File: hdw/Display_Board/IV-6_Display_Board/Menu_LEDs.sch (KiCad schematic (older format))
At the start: 1 part

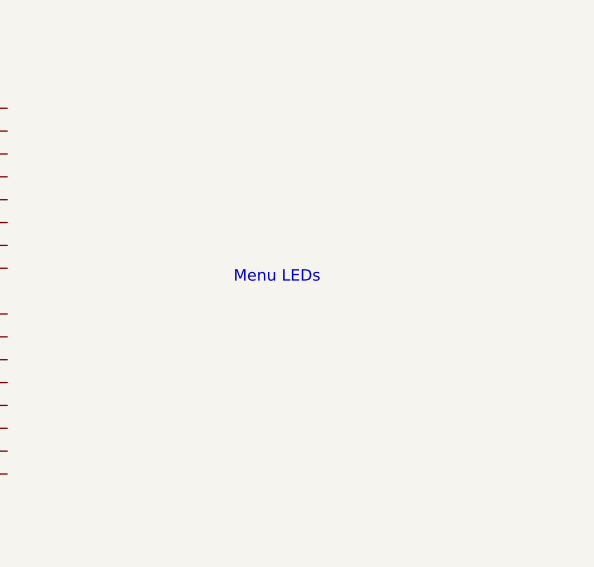
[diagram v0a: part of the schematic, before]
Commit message: Added backup RTC, IO connector, other stuff
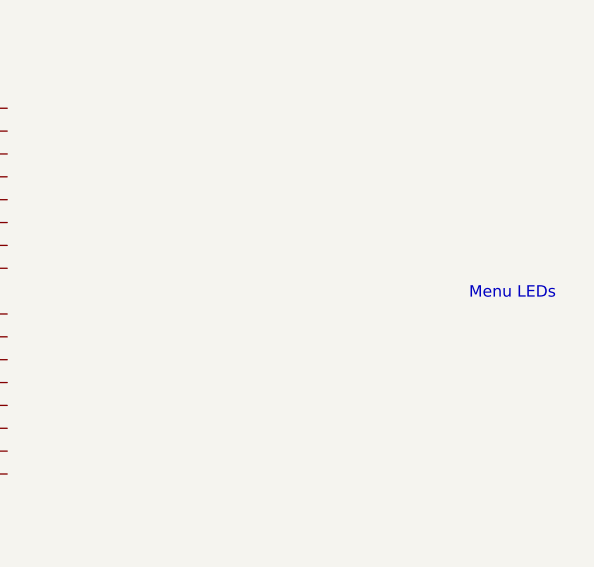
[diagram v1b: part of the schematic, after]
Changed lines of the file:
@@
 EESchema Schematic File Version 4
+LIBS:IV-6_Display_Board-cache
 EELAYER 30 0
 EELAYER END
 $Descr A 11000 8500
 encoding utf-8
-Sheet 5 5
+Sheet 5 7
 Title ""
 Date ""
@@
 Text GLabel 4360 2610 0    50   Input ~ 0
 I2C_DSP_SCL
-Text Notes 6750 3280 0    50   ~ 0
+Text Notes 7780 3350 0    50   ~ 0
 Menu LEDs
 $EndSCHEMATC

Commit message: Display board tweaks, added buzzer, other stuff
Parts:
- added C?: 0.1uF, Capacitors_SMD:C_0603, symbol Custom_Library:C_Custom
- added DOC?: I2C_Address, symbol Custom_Library:I2C_Address
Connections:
- net +5V: now also C?.1
- net GND: now also C?.2
- net Display_Time_LED: now reaches U?.1 (P00)
- net 24HR_Mode_LED: now reaches U?.10 (P10)
- net Alarm_Enable_LED: now reaches U?.11 (P11)
- net Set_Time_LED: now reaches U?.2 (P01)
- net Display_Date_LED: now reaches U?.3 (P02)
- net Set_Date_LED: now reaches U?.4 (P03)
- net Display_Weekday_LED: now reaches U?.5 (P04)
- net Set_Weekday_LED: now reaches U?.6 (P05)
- net Display_Alarm_LED: now reaches U?.7 (P06)
- net Set_Alarm_LED: now reaches U?.8 (P07)
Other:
- note removed: "Menu LEDs"
- moved on the sheet: U?
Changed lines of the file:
@@
 $Descr A 11000 8500
 encoding utf-8
-Sheet 5 9
+Sheet 5 12
 Title ""
 Date ""
@@
 L Interface_Expansion:TCA9555RGER U?
 U 1 1 5E0AA272
-P 5060 3310
-F 0 "U?" H 4610 4260 50  0000 C CNN
-F 1 "TCA9555RGER" H 5060 3310 50  0000 C CNN
-F 2 "Package_DFN_QFN:QFN-24-1EP_4x4mm_P0.5mm_EP2.6x2.6mm" H 6260 2310 50  0001 C CNN
-F 3 "http://www.ti.com/lit/ds/symlink/tca9555.pdf" H 4560 4210 50  0001 C CNN
-	1    5060 3310
+P 2960 3100
+F 0 "U?" H 2510 4050 50  0000 C CNN
+F 1 "TCA9555RGER" H 2960 3100 50  0000 C CNN
+F 2 "Package_DFN_QFN:QFN-24-1EP_4x4mm_P0.5mm_EP2.6x2.6mm" H 4160 2100 50  0001 C CNN
+F 3 "http://www.ti.com/lit/ds/symlink/tca9555.pdf" H 2460 4000 50  0001 C CNN
+	1    2960 3100
 	1    0    0    -1
 $EndComp
@@
 L power:+5V #PWR?
 U 1 1 5E0AB497
-P 5060 2210
-F 0 "#PWR?" H 5060 2060 50  0001 C CNN
-F 1 "+5V" H 5060 2350 50  0000 C CNN
-F 2 "" H 5060 2210 50  0001 C CNN
-F 3 "" H 5060 2210 50  0001 C CNN
-	1    5060 2210
+P 2960 2000
+F 0 "#PWR?" H 2960 1850 50  0001 C CNN
+F 1 "+5V" H 2960 2140 50  0000 C CNN
+F 2 "" H 2960 2000 50  0001 C CNN
+F 3 "" H 2960 2000 50  0001 C CNN
+	1    2960 2000
 	1    0    0    -1
 $EndComp
@@
 L power:GND #PWR?
 U 1 1 5E0AB88F
-P 5110 4490
-F 0 "#PWR?" H 5110 4240 50  0001 C CNN
-F 1 "GND" H 5110 4340 50  0000 C CNN
-F 2 "" H 5110 4490 50  0001 C CNN
-F 3 "" H 5110 4490 50  0001 C CNN
-	1    5110 4490
+P 3010 4280
+F 0 "#PWR?" H 3010 4030 50  0001 C CNN
+F 1 "GND" H 3010 4130 50  0000 C CNN
+F 2 "" H 3010 4280 50  0001 C CNN
+F 3 "" H 3010 4280 50  0001 C CNN
+	1    3010 4280
 	1    0    0    -1
 $EndComp
 Wire Wire Line
-	5110 4490 5110 4450
+	3010 4280 3010 4240
 Wire Wire Line
-	5110 4450 5060 4450
+	3010 4240 2960 4240
 Wire Wire Line
-	5060 4450 5060 4410
+	2960 4240 2960 4200
 Wire Wire Line
-	5110 4450 5160 4450
+	3010 4240 3060 4240
 Wire Wire Line
-	5160 4450 5160 4410
-Connection ~ 5110 4450
-NoConn ~ 4360 2710
-Text GLabel 4360 2510 0    50   BiDi ~ 0
+	3060 4240 3060 4200
+Connection ~ 3010 4240
+NoConn ~ 2260 2500
+Text GLabel 2260 2300 0    50   BiDi ~ 0
 I2C_DSP_SDA
-Text GLabel 4360 2610 0    50   Input ~ 0
+Text GLabel 2260 2400 0    50   Input ~ 0
 I2C_DSP_SCL
-Text Notes 7780 3350 0    50   ~ 0
-Menu LEDs
+Text GLabel 3660 3200 2    50   Output ~ 0
+24HR_Mode_LED
+Text GLabel 3660 2300 2    50   Output ~ 0
+Display_Time_LED
+Text GLabel 3660 2500 2    50   Output ~ 0
+Display_Date_LED
+Text GLabel 3660 2900 2    50   Output ~ 0
+Display_Alarm_LED
+Text GLabel 3660 2400 2    50   Output ~ 0
+Set_Time_LED
+Text GLabel 3660 2600 2    50   Output ~ 0
+Set_Date_LED
+Text GLabel 3660 3000 2    50   Output ~ 0
+Set_Alarm_LED
+Text GLabel 3660 2700 2    50   Output ~ 0
+Display_Weekday_LED
+Text GLabel 3660 2800 2    50   Output ~ 0
+Set_Weekday_LED
+$Comp
+L Custom_Library:I2C_Address DOC?
+U 1 1 5E3D77B3
+P 4030 4480
+F 0 "DOC?" H 4030 4730 60  0001 C CNN
+F 1 "I2C_Address" H 3580 4480 60  0000 L CNN
+F 2 "" H 4030 4830 60  0001 C CNN
+F 3 "" H 4030 4830 60  0001 C CNN
+	1    4030 4480
+	1    0    0    -1
+$EndComp
+Text GLabel 3660 3300 2    50   Output ~ 0
+Alarm_Enable_LED
+$Comp
+L Custom_Library:C_Custom C?
+U 1 1 5E25E93E
+P 2920 5060
+AR Path="/5C1D5CD8/5E25E93E" Ref="C?"  Part="1"
+AR Path="/5C1D5CCA/5E25E93E" Ref="C?"  Part="1"
+AR Path="/5C26E09A/5E25E93E" Ref="C?"  Part="1"
+AR Path="/5D739492/5E25E93E" Ref="C?"  Part="1"
+AR Path="/5E28CFDF/5E25E93E" Ref="C?"  Part="1"
+AR Path="/5E36CE18/5E25E93E" Ref="C?"  Part="1"
+AR Path="/5E3C80C8/5E25E93E" Ref="C?"  Part="1"
+AR Path="/5E3C97B4/5E25E93E" Ref="C?"  Part="1"
+AR Path="/5E0A7959/5E25E93E" Ref="C?"  Part="1"
+F 0 "C?" H 2945 5160 50  0000 L CNN
+F 1 "0.1uF" H 2945 4960 50  0000 L CNN
+F 2 "Capacitors_SMD:C_0603" H 2958 4910 50  0001 C CNN
+F 3 "" H 2945 5160 50  0001 C CNN
+F 4 "311-1344-1-ND" H 3345 5560 60  0001 C CNN "Digi-Key PN"
+F 5 "0603" H 2770 5160 50  0000 R CNN "display_footprint"
+F 6 "50V" H 2770 5060 50  0000 R CNN "Voltage"
+F 7 "X7R" H 2770 4960 50  0000 R CNN "Dielectric"
+	1    2920 5060
+	-1   0    0    -1
+$EndComp
+$Comp
+L power:GND #PWR?
+U 1 1 5E25E944
+P 2920 5210
+AR Path="/5E28CFDF/5E25E944" Ref="#PWR?"  Part="1"
+AR Path="/5E36CE18/5E25E944" Ref="#PWR?"  Part="1"
+AR Path="/5E3C80C8/5E25E944" Ref="#PWR?"  Part="1"
+AR Path="/5E3C97B4/5E25E944" Ref="#PWR?"  Part="1"
+AR Path="/5E0A7959/5E25E944" Ref="#PWR?"  Part="1"
+F 0 "#PWR?" H 2920 4960 50  0001 C CNN
+F 1 "GND" H 2920 5060 50  0000 C CNN
+F 2 "" H 2920 5210 50  0001 C CNN
+F 3 "" H 2920 5210 50  0001 C CNN
+	1    2920 5210
+	1    0    0    -1
+$EndComp
+$Comp
+L power:+5V #PWR?
+U 1 1 5E25E974
+P 2920 4910
+F 0 "#PWR?" H 2920 4760 50  0001 C CNN
+F 1 "+5V" H 2920 5050 50  0000 C CNN
+F 2 "" H 2920 4910 50  0001 C CNN
+F 3 "" H 2920 4910 50  0001 C CNN
+	1    2920 4910
+	1    0    0    -1
+$EndComp
 $EndSCHEMATC

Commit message: Few hdw tweaks
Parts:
- added D? (x10): Cyan, symbol Device:LED
- added R? (x10): 499, Resistors_SMD:R_0603, symbol Custom_Library:R_Custom
- DOC?: value I2C_Address -> 0x20
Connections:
- net 24HR_Mode_LED: now also U?.11 (P11), R?.1; no longer U?.10 (P10)
- net Alarm_Enable_LED: now also U?.10 (P10), R?.1; no longer U?.11 (P11)
- net Display_Alarm_LED: now also R?.1
- net Display_Date_LED: now also R?.1
- net Display_Time_LED: now also R?.1
- net Display_Weekday_LED: now also R?.1
- net GND: now also U?.18 (A0), U?.23 (A1), U?.24 (A2), D?.1 (K), D?.1 (K), D?.1 (K), D?.1 (K), D?.1 (K), D?.1 (K), D?.1 (K), D?.1 (K), D?.1 (K), D?.1 (K)
- net Set_Alarm_LED: now also R?.1
- net Set_Date_LED: now also R?.1
- net Set_Time_LED: now also R?.1
- net Set_Weekday_LED: now also R?.1
- new net: D?.2 (A), R?.2 (x10)

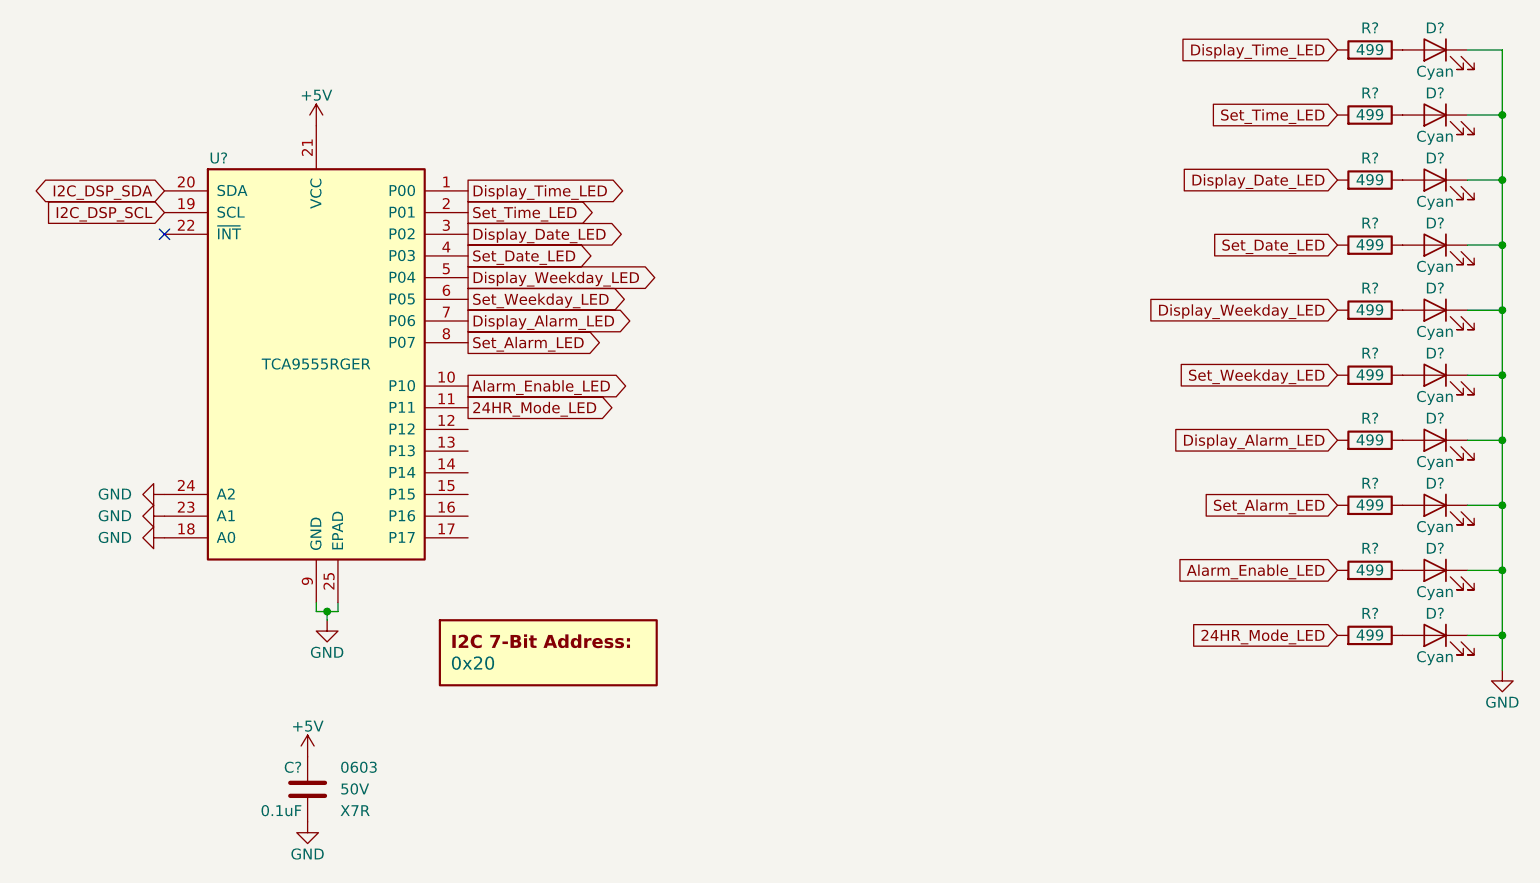
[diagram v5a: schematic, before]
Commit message: Started display board PCB
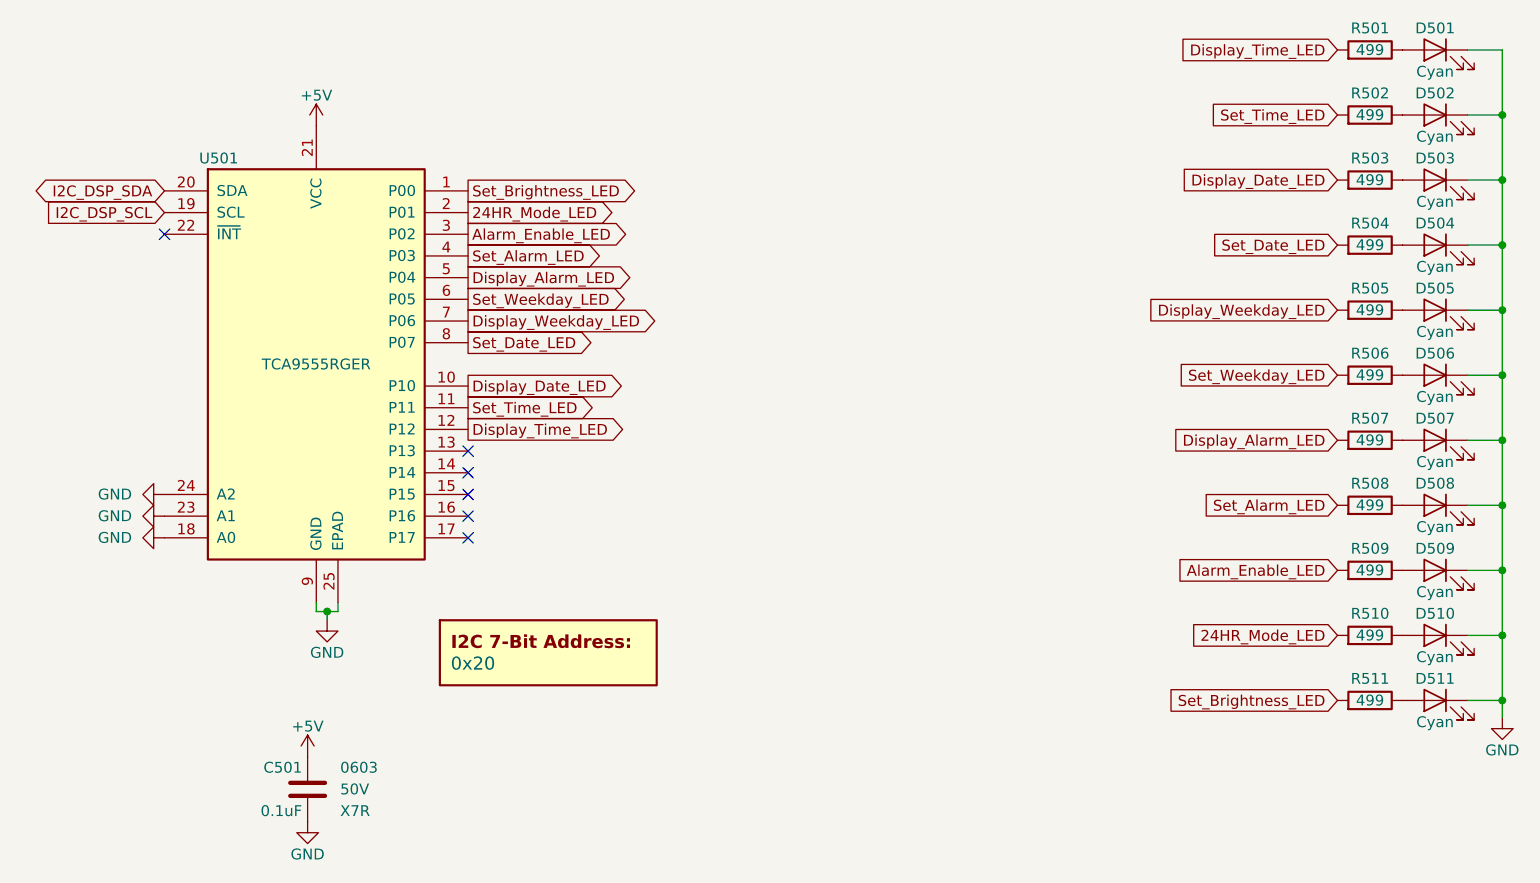
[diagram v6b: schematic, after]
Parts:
- added D511: Cyan, LEDs:LED_0603, symbol Device:LED
- added R511: 499, Resistors_SMD:R_0603, symbol Custom_Library:R_Custom
- D501, D502, D503, D504, D505, D506, D507, D508, D509, D510: renamed from D?; footprint (none) -> LEDs:LED_0603
- gave numbers to parts that had none: 13
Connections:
- net 24HR_Mode_LED: now also U501.2 (P01); no longer U501.11 (P11)
- net Alarm_Enable_LED: now also U501.3 (P02); no longer U501.10 (P10)
- net Display_Alarm_LED: now also U501.5 (P04); no longer U501.7 (P06)
- net Display_Date_LED: now also U501.10 (P10); no longer U501.3 (P02)
- net Display_Time_LED: now also U501.12 (P12); no longer U501.1 (P00)
- net Display_Weekday_LED: now also U501.7 (P06); no longer U501.5 (P04)
- net GND: now also D511.1 (K)
- net Set_Alarm_LED: now also U501.4 (P03); no longer U501.8 (P07)
- net Set_Date_LED: now also U501.8 (P07); no longer U501.4 (P03)
- net Set_Time_LED: now also U501.11 (P11); no longer U501.2 (P01)
- new net: D511.2 (A), R511.2
- new net Set_Brightness_LED: R511.1, U501.1 (P00)
- no-connect marks 1 -> 6

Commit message: Finished IV-6 layout, generated gerbers, BOM
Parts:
- D501, D502, D503, D504, D505, D506, D507, D508, D509, D510, D511: Digi-Key PN (none) -> 754-2180-1-ND
- U501: Digi-Key PN (none) -> 296-44537-1-ND
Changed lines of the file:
@@
 F 2 "Package_DFN_QFN:QFN-24-1EP_4x4mm_P0.5mm_EP2.6x2.6mm" H 4160 2100 50  0001 C CNN
 F 3 "http://www.ti.com/lit/ds/symlink/tca9555.pdf" H 2460 4000 50  0001 C CNN
+F 4 "296-44537-1-ND" H 2960 3100 50  0001 C CNN "Digi-Key PN"
 	1    2960 3100
 	1    0    0    -1
@@
 F 2 "LEDs:LED_0603" H 8120 1650 50  0001 C CNN
 F 3 "~" H 8120 1650 50  0001 C CNN
+F 4 "754-2180-1-ND" H 8120 1650 50  0001 C CNN "Digi-Key PN"
 	1    8120 1650
 	-1   0    0    -1
@@
 F 2 "LEDs:LED_0603" H 8120 1950 50  0001 C CNN
 F 3 "~" H 8120 1950 50  0001 C CNN
+F 4 "754-2180-1-ND" H 8120 1950 50  0001 C CNN "Digi-Key PN"
 	1    8120 1950
 	-1   0    0    -1
@@
 F 2 "LEDs:LED_0603" H 8120 2250 50  0001 C CNN
 F 3 "~" H 8120 2250 50  0001 C CNN
+F 4 "754-2180-1-ND" H 8120 2250 50  0001 C CNN "Digi-Key PN"
 	1    8120 2250
 	-1   0    0    -1
@@
 F 2 "LEDs:LED_0603" H 8120 2550 50  0001 C CNN
 F 3 "~" H 8120 2550 50  0001 C CNN
+F 4 "754-2180-1-ND" H 8120 2550 50  0001 C CNN "Digi-Key PN"
 	1    8120 2550
 	-1   0    0    -1
@@
 F 2 "LEDs:LED_0603" H 8120 2850 50  0001 C CNN
 F 3 "~" H 8120 2850 50  0001 C CNN
+F 4 "754-2180-1-ND" H 8120 2850 50  0001 C CNN "Digi-Key PN"
 	1    8120 2850
 	-1   0    0    -1
@@
 F 2 "LEDs:LED_0603" H 8120 3150 50  0001 C CNN
 F 3 "~" H 8120 3150 50  0001 C CNN
+F 4 "754-2180-1-ND" H 8120 3150 50  0001 C CNN "Digi-Key PN"
 	1    8120 3150
 	-1   0    0    -1
@@
 F 2 "LEDs:LED_0603" H 8120 3450 50  0001 C CNN
 F 3 "~" H 8120 3450 50  0001 C CNN
+F 4 "754-2180-1-ND" H 8120 3450 50  0001 C CNN "Digi-Key PN"
 	1    8120 3450
 	-1   0    0    -1
@@
 F 2 "LEDs:LED_0603" H 8120 3750 50  0001 C CNN
 F 3 "~" H 8120 3750 50  0001 C CNN
+F 4 "754-2180-1-ND" H 8120 3750 50  0001 C CNN "Digi-Key PN"
 	1    8120 3750
 	-1   0    0    -1
@@
 F 2 "LEDs:LED_0603" H 8120 4050 50  0001 C CNN
 F 3 "~" H 8120 4050 50  0001 C CNN
+F 4 "754-2180-1-ND" H 8120 4050 50  0001 C CNN "Digi-Key PN"
 	1    8120 4050
 	-1   0    0    -1
@@
 F 2 "LEDs:LED_0603" H 8120 4350 50  0001 C CNN
 F 3 "~" H 8120 4350 50  0001 C CNN
+F 4 "754-2180-1-ND" H 8120 4350 50  0001 C CNN "Digi-Key PN"
 	1    8120 4350
 	-1   0    0    -1
@@
 F 2 "LEDs:LED_0603" H 8120 4650 50  0001 C CNN
 F 3 "~" H 8120 4650 50  0001 C CNN
+F 4 "754-2180-1-ND" H 8120 4650 50  0001 C CNN "Digi-Key PN"
 	1    8120 4650
 	-1   0    0    -1
